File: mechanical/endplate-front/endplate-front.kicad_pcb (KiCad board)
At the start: 2 copper layers, 88 x 38 mm, 0 parts

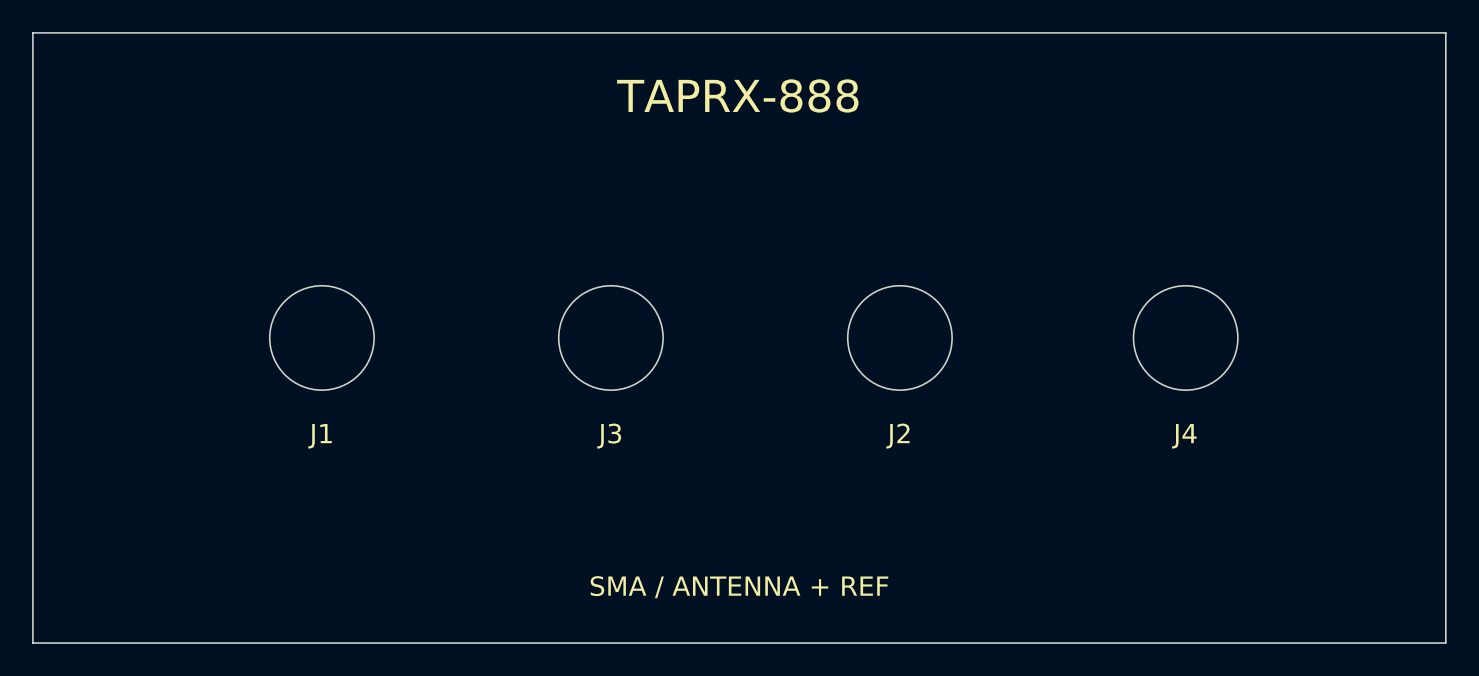
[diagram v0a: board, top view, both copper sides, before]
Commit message: mechanical: rebuild end plates from enclosure DXF geometry
Replace the nominal 88x38 starter outline with real geometry sectioned from the
enclosure extrusion end (FreeCAD DXF, centred on 0,0):

- outline 88x38 mm, corner radius 4.5 (rounded rect: 4 edges + 4 arcs)
- four M3 corner mounting holes, Ø3.4 at (±41, ±14.21) -> the plate screws on;
  it is not a slide-in panel (the 84.2 mm groove is the internal PCB slot)

Connector cutout X's are the main board's real connector positions mapped to
plate-centred coords (plate-X = 44 + (board-X - 138)), verified against the PCB:

- front SMA J1/J3/J2/J4 at -27/-9/+9/+26.8 mm from centre
- rear USB J5 at +19 mm from centre; J11 (JTAG) internal, no cutout

Connector Y remains a placeholder at plate centre pending the PCB rail height +
connector centre heights (3D models); cutout sizes (SMA Ø6.5, USB 13x11) and the
rear X-mirror stay flagged on Cmts.User. Open in KiCad 10 to confirm it parses.

Co-Authored-By: Claude Opus 4.8 <noreply@anthropic.com>
Claude-Session: https://claude.ai/code/session_019A4jkTeNPLki8CdfTWEUwM
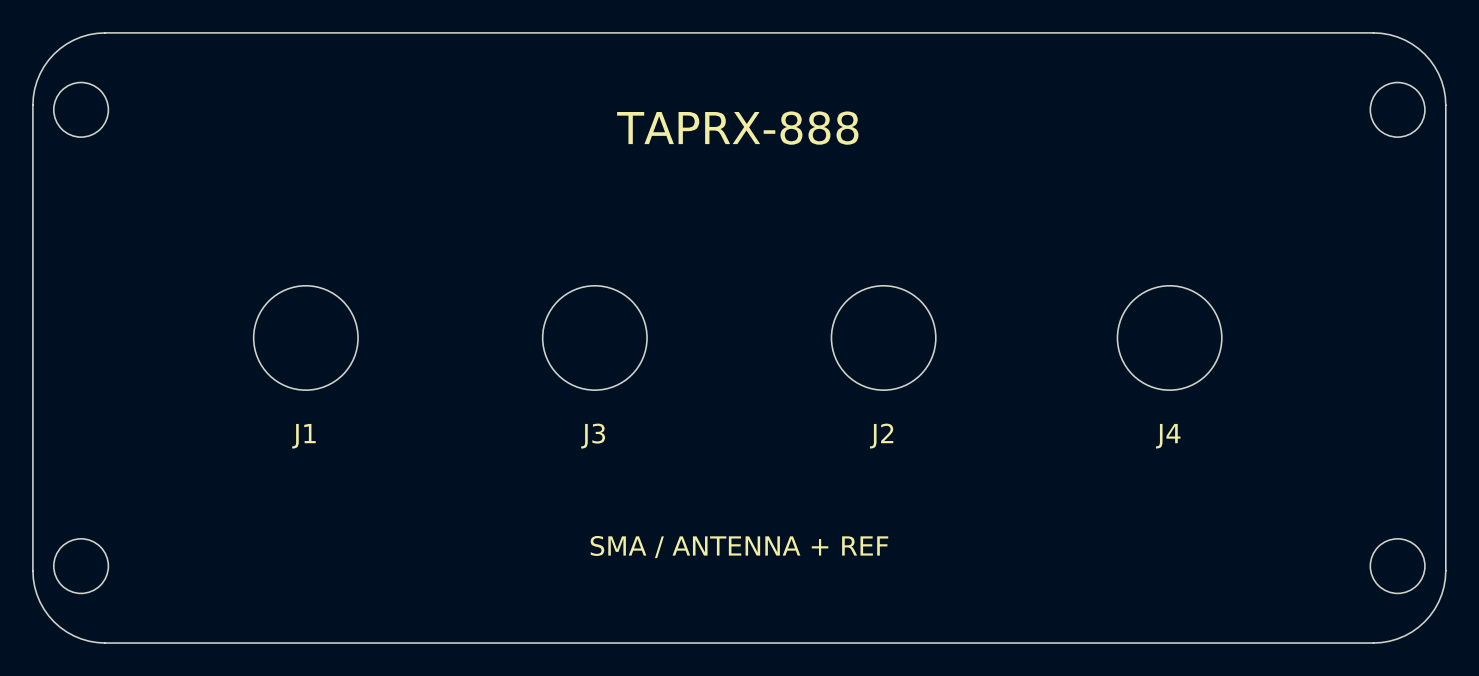
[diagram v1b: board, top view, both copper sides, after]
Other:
- outline, holes or cut-outs redrawn
- board text added: "Outline+M3 corner holes from enclosure DXF (88x38 R4.5, holes Ø3.4 @ +/-41,+/-14.21). CONNECTOR Y IS PLACEHOLDER at plate centre -- set from PCB rail height + connector centre heights (3D models). SMA Ø6.5 / USB 13x11 verify vs parts. Open in KiCad 10 to confirm parse."
- board text removed: "PLACEHOLDER GEOMETRY - verify vs enclosure STEP: plate 88x38 nominal (check groove fit); connector Y at plate centre (needs board height in rail + connector centre height); SMA D6.5 / USB 13x11 (verify vs parts)."
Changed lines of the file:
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@@
 		(company "TAPR")
 		(comment 1 "Non-functional enclosure end plate")
-		(comment 2 "Starter geometry -- verify against enclosure STEP")
+		(comment 2 "Outline+holes from enclosure DXF; connector Y placeholder")
 	)
 	(layers
@@
 	(net 0 "")
 	(gr_line
-		(start 0 0)
-		(end 88.0 0)
-		(stroke
-			(width 0.1)
-			(type default)
-		)
-		(layer "Edge.Cuts")
-	)
-	(gr_line
-		(start 88.0 0)
-		(end 88.0 38.0)
-		(stroke
-			(width 0.1)
-			(type default)
-		)
-		(layer "Edge.Cuts")
-	)
-	(gr_line
-		(start 88.0 38.0)
-		(end 0 38.0)
-		(stroke
-			(width 0.1)
-			(type default)
-		)
-		(layer "Edge.Cuts")
-	)
-	(gr_line
-		(start 0 38.0)
-		(end 0 0)
-		(stroke
-			(width 0.1)
-			(type default)
-		)
-		(layer "Edge.Cuts")
-	)
-	(gr_circle
-		(center 18.0 19.0)
-		(end 21.25 19.0)
+		(start 4.5 0)
+		(end 83.5 0)
+		(stroke
+			(width 0.1)
+			(type default)
+		)
+		(layer "Edge.Cuts")
+	)
+	(gr_line
+		(start 88.0 4.5)
+		(end 88.0 33.5)
+		(stroke
+			(width 0.1)
+			(type default)
+		)
+		(layer "Edge.Cuts")
+	)
+	(gr_line
+		(start 83.5 38.0)
+		(end 4.5 38.0)
+		(stroke
+			(width 0.1)
+			(type default)
+		)
+		(layer "Edge.Cuts")
+	)
+	(gr_line
+		(start 0 33.5)
+		(end 0 4.5)
+		(stroke
+			(width 0.1)
+			(type default)
+		)
+		(layer "Edge.Cuts")
+	)
+	(gr_arc
+		(start 0 4.5)
+		(mid 1.318 1.318)
+		(end 4.5 0)
+		(stroke
+			(width 0.1)
+			(type default)
+		)
+		(layer "Edge.Cuts")
+	)
+	(gr_arc
+		(start 83.5 0)
+		(mid 86.682 1.318)
+		(end 88.0 4.5)
+		(stroke
+			(width 0.1)
+			(type default)
+		)
+		(layer "Edge.Cuts")
+	)
+	(gr_arc
+		(start 88.0 33.5)
+		(mid 86.682 36.682)
+		(end 83.5 38.0)
+		(stroke
+			(width 0.1)
+			(type default)
+		)
+		(layer "Edge.Cuts")
+	)
+	(gr_arc
+		(start 4.5 38.0)
+		(mid 1.318 36.682)
+		(end 0 33.5)
+		(stroke
+			(width 0.1)
+			(type default)
+		)
+		(layer "Edge.Cuts")
+	)
+	(gr_circle
+		(center 3.0 4.79)
+		(end 4.7 4.79)
+		(stroke
+			(width 0.1)
+			(type default)
+		)
+		(fill no)
+		(layer "Edge.Cuts")
+	)
+	(gr_circle
+		(center 85.0 4.79)
+		(end 86.7 4.79)
+		(stroke
+			(width 0.1)
+			(type default)
+		)
+		(fill no)
+		(layer "Edge.Cuts")
+	)
+	(gr_circle
+		(center 3.0 33.21)
+		(end 4.7 33.21)
+		(stroke
+			(width 0.1)
+			(type default)
+		)
+		(fill no)
+		(layer "Edge.Cuts")
+	)
+	(gr_circle
+		(center 85.0 33.21)
+		(end 86.7 33.21)
+		(stroke
+			(width 0.1)
+			(type default)
+		)
+		(fill no)
+		(layer "Edge.Cuts")
+	)
+	(gr_circle
+		(center 17.0 19.0)
+		(end 20.25 19.0)
 		(stroke
 			(width 0.1)
@@
 	)
 	(gr_text "J1"
-		(at 18.0 25.0)
-		(layer "F.SilkS")
-		(effects
-			(font
-				(size 1.2 1.2)
-				(thickness 0.2)
-			)
-		)
-	)
-	(gr_circle
-		(center 36.0 19.0)
-		(end 39.25 19.0)
+		(at 17.0 25.0)
+		(layer "F.SilkS")
+		(effects
+			(font
+				(size 1.2 1.2)
+				(thickness 0.2)
+			)
+		)
+	)
+	(gr_circle
+		(center 35.0 19.0)
+		(end 38.25 19.0)
 		(stroke
 			(width 0.1)
@@
 	)
 	(gr_text "J3"
-		(at 36.0 25.0)
-		(layer "F.SilkS")
-		(effects
-			(font
-				(size 1.2 1.2)
-				(thickness 0.2)
-			)
-		)
-	)
-	(gr_circle
-		(center 54.0 19.0)
-		(end 57.25 19.0)
+		(at 35.0 25.0)
+		(layer "F.SilkS")
+		(effects
+			(font
+				(size 1.2 1.2)
+				(thickness 0.2)
+			)
+		)
+	)
+	(gr_circle
+		(center 52.986 19.0)
+		(end 56.236 19.0)
 		(stroke
 			(width 0.1)
@@
 	)
 	(gr_text "J2"
-		(at 54.0 25.0)
-		(layer "F.SilkS")
-		(effects
-			(font
-				(size 1.2 1.2)
-				(thickness 0.2)
-			)
-		)
-	)
-	(gr_circle
-		(center 71.8 19.0)
-		(end 75.05 19.0)
+		(at 52.986 25.0)
+		(layer "F.SilkS")
+		(effects
+			(font
+				(size 1.2 1.2)
+				(thickness 0.2)
+			)
+		)
+	)
+	(gr_circle
+		(center 70.8 19.0)
+		(end 74.05 19.0)
 		(stroke
 			(width 0.1)
@@
 	)
 	(gr_text "J4"
-		(at 71.8 25.0)
+		(at 70.8 25.0)
 		(layer "F.SilkS")
 		(effects
@@
 	)
 	(gr_text "TAPRX-888"
-		(at 44.0 4)
+		(at 44.0 6.0)
 		(layer "F.SilkS")
 		(effects
@@
 	)
 	(gr_text "SMA / ANTENNA + REF"
-		(at 44.0 34.5)
-		(layer "F.SilkS")
-		(effects
-			(font
-				(size 1.2 1.2)
-				(thickness 0.2)
-			)
-		)
-	)
-	(gr_text "PLACEHOLDER GEOMETRY - verify vs enclosure STEP: plate 88x38 nominal (check groove fit); connector Y at plate centre (needs board height in rail + connector centre height); SMA D6.5 / USB 13x11 (verify vs parts)."
+		(at 44.0 32.0)
+		(layer "F.SilkS")
+		(effects
+			(font
+				(size 1.2 1.2)
+				(thickness 0.2)
+			)
+		)
+	)
+	(gr_text "Outline+M3 corner holes from enclosure DXF (88x38 R4.5, holes Ø3.4 @ +/-41,+/-14.21). CONNECTOR Y IS PLACEHOLDER at plate centre -- set from PCB rail height + connector centre heights (3D models). SMA Ø6.5 / USB 13x11 verify vs parts. Open in KiCad 10 to confirm parse."
 		(at 44.0 42.0)
 		(layer "Cmts.User")

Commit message: mechanical: set end-plate connector Y from measured 7.9mm rail height
Drop the connector cutouts from their placeholder plate-centre position to their
real vertical location: the PCB rail sits 7.9mm above the enclosure floor
(measured), so with the floor at the plate's bottom edge the connector centres
land at plate Y = 30.12 (front SMA holes and rear USB opening alike). Add an
'ENCLOSURE FLOOR' silk marker on the bottom edge to pin orientation, and bump the
outline to the measured 38.02mm height. Connectors clear the bottom corner screws
(those sit at the far corners).

The SMA axis is ~the board plane; a USB connector body sits above the board
plane, so that opening's centre rises once the connector height is known -- left
flagged with the cutout-size placeholders (SMA Ø6.5 / USB 13x11) and the rear
X-mirror. README updated: connector Y is now set, not a placeholder.

Co-Authored-By: Claude Opus 4.8 <noreply@anthropic.com>
Claude-Session: https://claude.ai/code/session_019A4jkTeNPLki8CdfTWEUwM
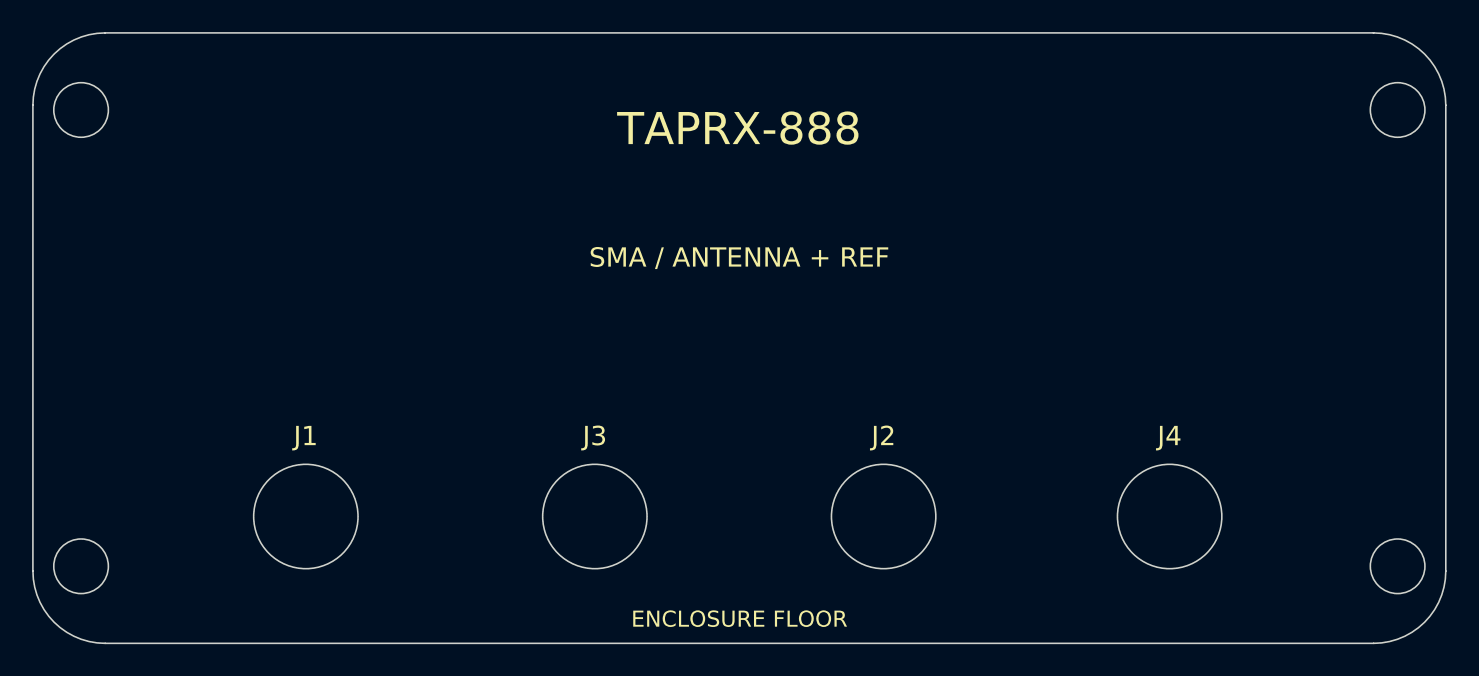
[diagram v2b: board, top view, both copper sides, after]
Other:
- outline, holes or cut-outs redrawn
- board text added: "ENCLOSURE FLOOR"
- board text added: "Outline+M3 corner holes from enclosure DXF (88x38 R4.5, holes Ø3.4 @ +/-41,+/-14.21). Connector Y set from measured 7.9mm PCB rail height above enclosure floor (bottom edge) -> plate Y 30.12. SMA axis ~board plane; USB opening sits ABOVE board plane by connector body height (part-specific, TBD). SMA Ø6.5 / USB 13x11 verify vs parts. Open in KiCad 10 to confirm parse."
- board text removed: "Outline+M3 corner holes from enclosure DXF (88x38 R4.5, holes Ø3.4 @ +/-41,+/-14.21). CONNECTOR Y IS PLACEHOLDER at plate centre -- set from PCB rail height + connector centre heights (3D models). SMA Ø6.5 / USB 13x11 verify vs parts. Open in KiCad 10 to confirm parse."
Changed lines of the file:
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@@
 	(gr_line
 		(start 88.0 4.5)
-		(end 88.0 33.5)
+		(end 88.0 33.52)
 		(stroke
 			(width 0.1)
@@
 	)
 	(gr_line
-		(start 83.5 38.0)
-		(end 4.5 38.0)
+		(start 83.5 38.02)
+		(end 4.5 38.02)
 		(stroke
 			(width 0.1)
@@
 	)
 	(gr_line
-		(start 0 33.5)
+		(start 0 33.52)
 		(end 0 4.5)
 		(stroke
@@
 	)
 	(gr_arc
-		(start 88.0 33.5)
-		(mid 86.682 36.682)
-		(end 83.5 38.0)
-		(stroke
-			(width 0.1)
-			(type default)
-		)
-		(layer "Edge.Cuts")
-	)
-	(gr_arc
-		(start 4.5 38.0)
-		(mid 1.318 36.682)
-		(end 0 33.5)
-		(stroke
-			(width 0.1)
-			(type default)
-		)
-		(layer "Edge.Cuts")
-	)
-	(gr_circle
-		(center 3.0 4.79)
-		(end 4.7 4.79)
-		(stroke
-			(width 0.1)
-			(type default)
-		)
-		(fill no)
-		(layer "Edge.Cuts")
-	)
-	(gr_circle
-		(center 85.0 4.79)
-		(end 86.7 4.79)
-		(stroke
-			(width 0.1)
-			(type default)
-		)
-		(fill no)
-		(layer "Edge.Cuts")
-	)
-	(gr_circle
-		(center 3.0 33.21)
-		(end 4.7 33.21)
-		(stroke
-			(width 0.1)
-			(type default)
-		)
-		(fill no)
-		(layer "Edge.Cuts")
-	)
-	(gr_circle
-		(center 85.0 33.21)
-		(end 86.7 33.21)
-		(stroke
-			(width 0.1)
-			(type default)
-		)
-		(fill no)
-		(layer "Edge.Cuts")
-	)
-	(gr_circle
-		(center 17.0 19.0)
-		(end 20.25 19.0)
+		(start 88.0 33.52)
+		(mid 86.682 36.702)
+		(end 83.5 38.02)
+		(stroke
+			(width 0.1)
+			(type default)
+		)
+		(layer "Edge.Cuts")
+	)
+	(gr_arc
+		(start 4.5 38.02)
+		(mid 1.318 36.702)
+		(end 0 33.52)
+		(stroke
+			(width 0.1)
+			(type default)
+		)
+		(layer "Edge.Cuts")
+	)
+	(gr_circle
+		(center 3.0 4.8)
+		(end 4.7 4.8)
+		(stroke
+			(width 0.1)
+			(type default)
+		)
+		(fill no)
+		(layer "Edge.Cuts")
+	)
+	(gr_circle
+		(center 85.0 4.8)
+		(end 86.7 4.8)
+		(stroke
+			(width 0.1)
+			(type default)
+		)
+		(fill no)
+		(layer "Edge.Cuts")
+	)
+	(gr_circle
+		(center 3.0 33.22)
+		(end 4.7 33.22)
+		(stroke
+			(width 0.1)
+			(type default)
+		)
+		(fill no)
+		(layer "Edge.Cuts")
+	)
+	(gr_circle
+		(center 85.0 33.22)
+		(end 86.7 33.22)
+		(stroke
+			(width 0.1)
+			(type default)
+		)
+		(fill no)
+		(layer "Edge.Cuts")
+	)
+	(gr_circle
+		(center 17.0 30.12)
+		(end 20.25 30.12)
 		(stroke
 			(width 0.1)
@@
 	)
 	(gr_text "J1"
-		(at 17.0 25.0)
-		(layer "F.SilkS")
-		(effects
-			(font
-				(size 1.2 1.2)
-				(thickness 0.2)
-			)
-		)
-	)
-	(gr_circle
-		(center 35.0 19.0)
-		(end 38.25 19.0)
+		(at 17.0 25.12)
+		(layer "F.SilkS")
+		(effects
+			(font
+				(size 1.2 1.2)
+				(thickness 0.2)
+			)
+		)
+	)
+	(gr_circle
+		(center 35.0 30.12)
+		(end 38.25 30.12)
 		(stroke
 			(width 0.1)
@@
 	)
 	(gr_text "J3"
-		(at 35.0 25.0)
-		(layer "F.SilkS")
-		(effects
-			(font
-				(size 1.2 1.2)
-				(thickness 0.2)
-			)
-		)
-	)
-	(gr_circle
-		(center 52.986 19.0)
-		(end 56.236 19.0)
+		(at 35.0 25.12)
+		(layer "F.SilkS")
+		(effects
+			(font
+				(size 1.2 1.2)
+				(thickness 0.2)
+			)
+		)
+	)
+	(gr_circle
+		(center 52.986 30.12)
+		(end 56.236 30.12)
 		(stroke
 			(width 0.1)
@@
 	)
 	(gr_text "J2"
-		(at 52.986 25.0)
-		(layer "F.SilkS")
-		(effects
-			(font
-				(size 1.2 1.2)
-				(thickness 0.2)
-			)
-		)
-	)
-	(gr_circle
-		(center 70.8 19.0)
-		(end 74.05 19.0)
+		(at 52.986 25.12)
+		(layer "F.SilkS")
+		(effects
+			(font
+				(size 1.2 1.2)
+				(thickness 0.2)
+			)
+		)
+	)
+	(gr_circle
+		(center 70.8 30.12)
+		(end 74.05 30.12)
 		(stroke
 			(width 0.1)
@@
 	)
 	(gr_text "J4"
-		(at 70.8 25.0)
+		(at 70.8 25.12)
 		(layer "F.SilkS")
 		(effects
@@
 	)
 	(gr_text "TAPRX-888"
-		(at 44.0 6.0)
+		(at 44.0 6)
 		(layer "F.SilkS")
 		(effects
@@
 	)
 	(gr_text "SMA / ANTENNA + REF"
-		(at 44.0 32.0)
-		(layer "F.SilkS")
-		(effects
-			(font
-				(size 1.2 1.2)
-				(thickness 0.2)
-			)
-		)
-	)
-	(gr_text "Outline+M3 corner holes from enclosure DXF (88x38 R4.5, holes Ø3.4 @ +/-41,+/-14.21). CONNECTOR Y IS PLACEHOLDER at plate centre -- set from PCB rail height + connector centre heights (3D models). SMA Ø6.5 / USB 13x11 verify vs parts. Open in KiCad 10 to confirm parse."
-		(at 44.0 42.0)
+		(at 44.0 14)
+		(layer "F.SilkS")
+		(effects
+			(font
+				(size 1.2 1.2)
+				(thickness 0.2)
+			)
+		)
+	)
+	(gr_text "ENCLOSURE FLOOR"
+		(at 44.0 36.52)
+		(layer "F.SilkS")
+		(effects
+			(font
+				(size 1.0 1.0)
+				(thickness 0.15)
+			)
+		)
+	)
+	(gr_text "Outline+M3 corner holes from enclosure DXF (88x38 R4.5, holes Ø3.4 @ +/-41,+/-14.21). Connector Y set from measured 7.9mm PCB rail height above enclosure floor (bottom edge) -> plate Y 30.12. SMA axis ~board plane; USB opening sits ABOVE board plane by connector body height (part-specific, TBD). SMA Ø6.5 / USB 13x11 verify vs parts. Open in KiCad 10 to confirm parse."
+		(at 44.0 42.02)
 		(layer "Cmts.User")
 		(effects
